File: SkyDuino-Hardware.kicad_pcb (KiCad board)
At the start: 4 copper layers, 123 x 56 mm, 75 parts, among them J1 24V, J11 DBG, J12 USB-A RMT, J13 DISP, J14 USB_C Artisan, J2 BT, J4 Drum, J5 Exhaust, J6 Cooling, J7 Cooling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

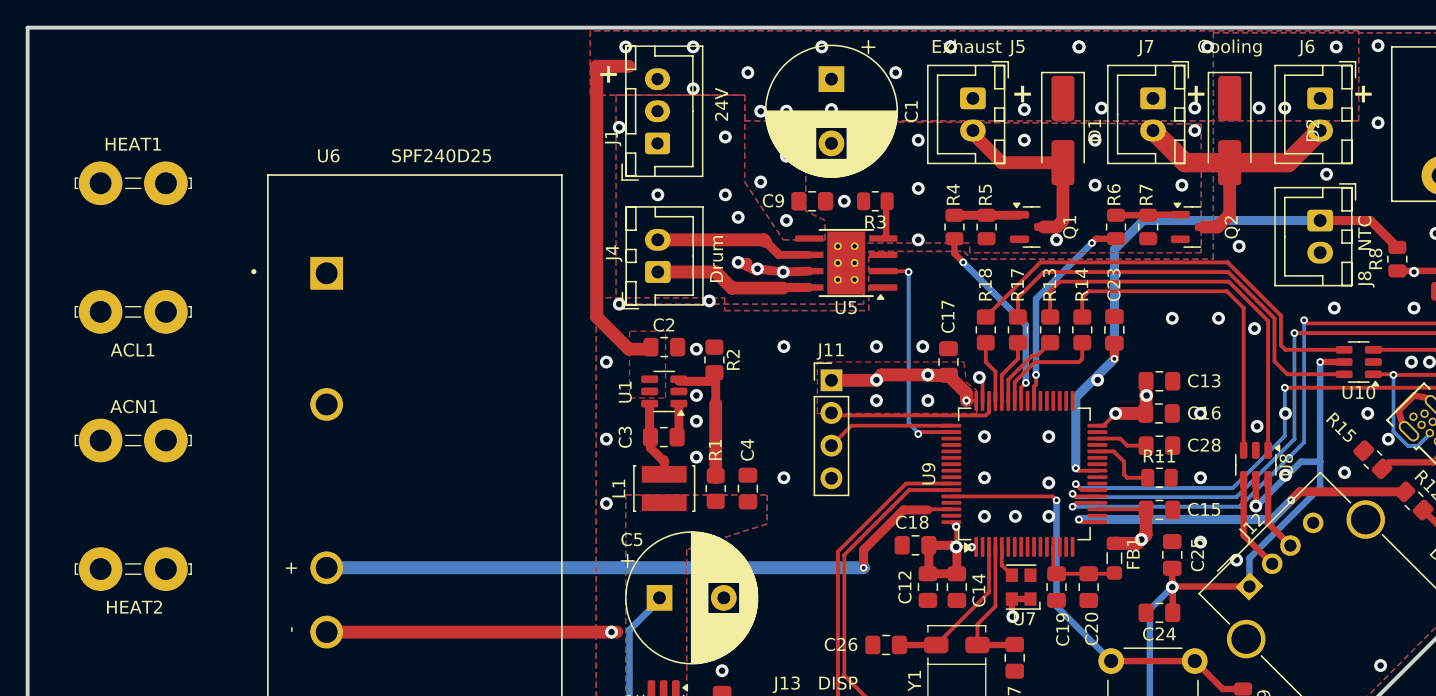
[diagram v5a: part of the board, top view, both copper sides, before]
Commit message: Label AC lines
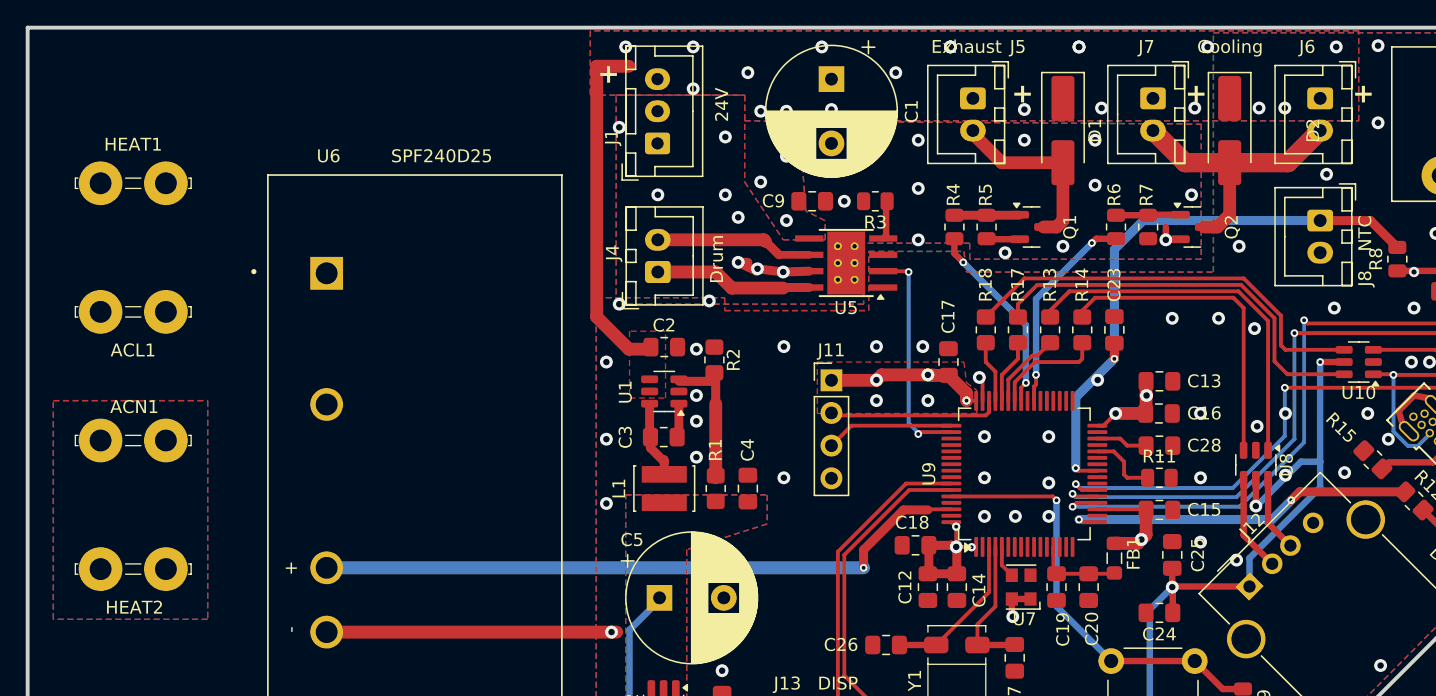
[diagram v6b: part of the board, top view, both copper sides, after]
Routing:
- net GND: track 32.5 -> 36.1 mm, vias 78 -> 79
- net Net-(R13-Pad1): track 30.6 -> 29.1 mm
- net Net-(R17-Pad1): track 32.9 -> 31.8 mm
- net Net-(R18-Pad1): track 33.8 -> 32.8 mm
- net Net-(R14-Pad1): track 25.9 -> 24.9 mm
- added copper zone on B.Cu, net Net-(ACN1-Pin_1)
- added copper zone on F.Cu, net Net-(ACN1-Pin_1)
- added copper zone on In1.Cu, net Net-(ACN1-Pin_1)
- added copper zone on In2.Cu, net Net-(ACN1-Pin_1)

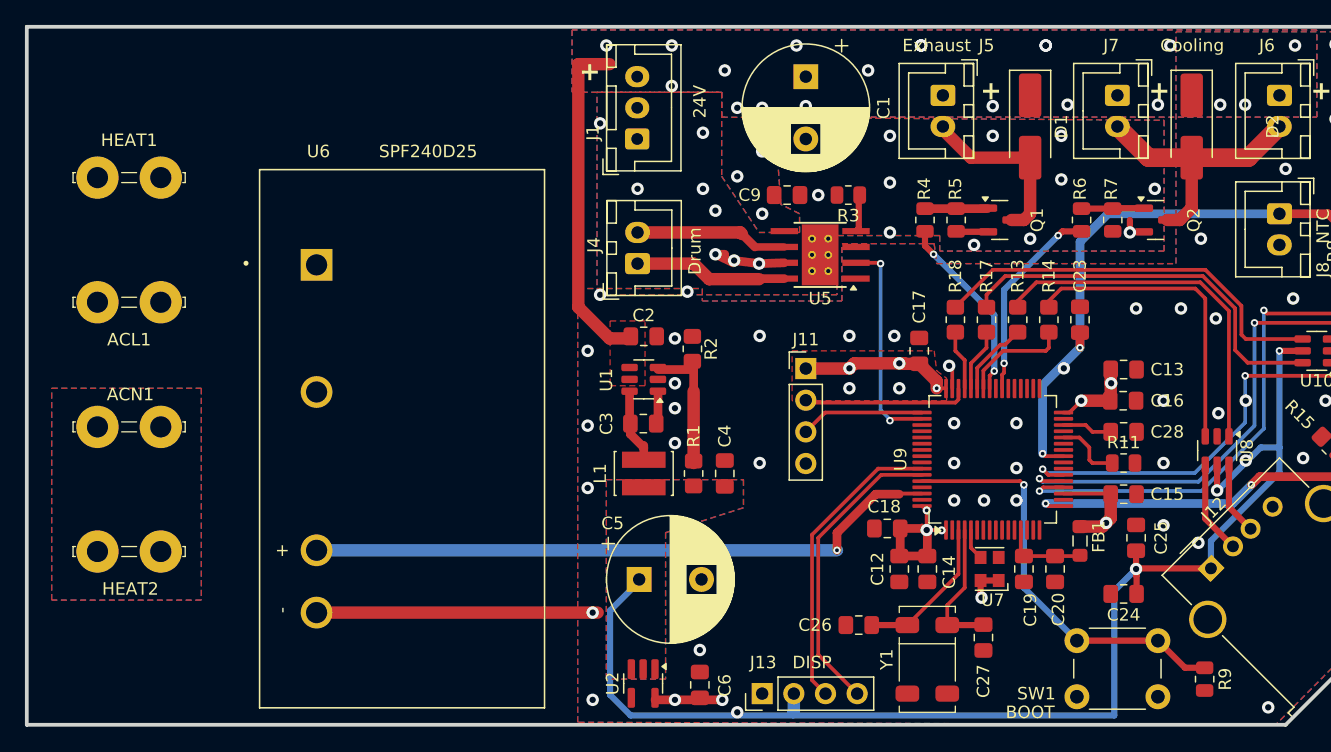
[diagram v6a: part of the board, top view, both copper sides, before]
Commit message: Pour AC lines
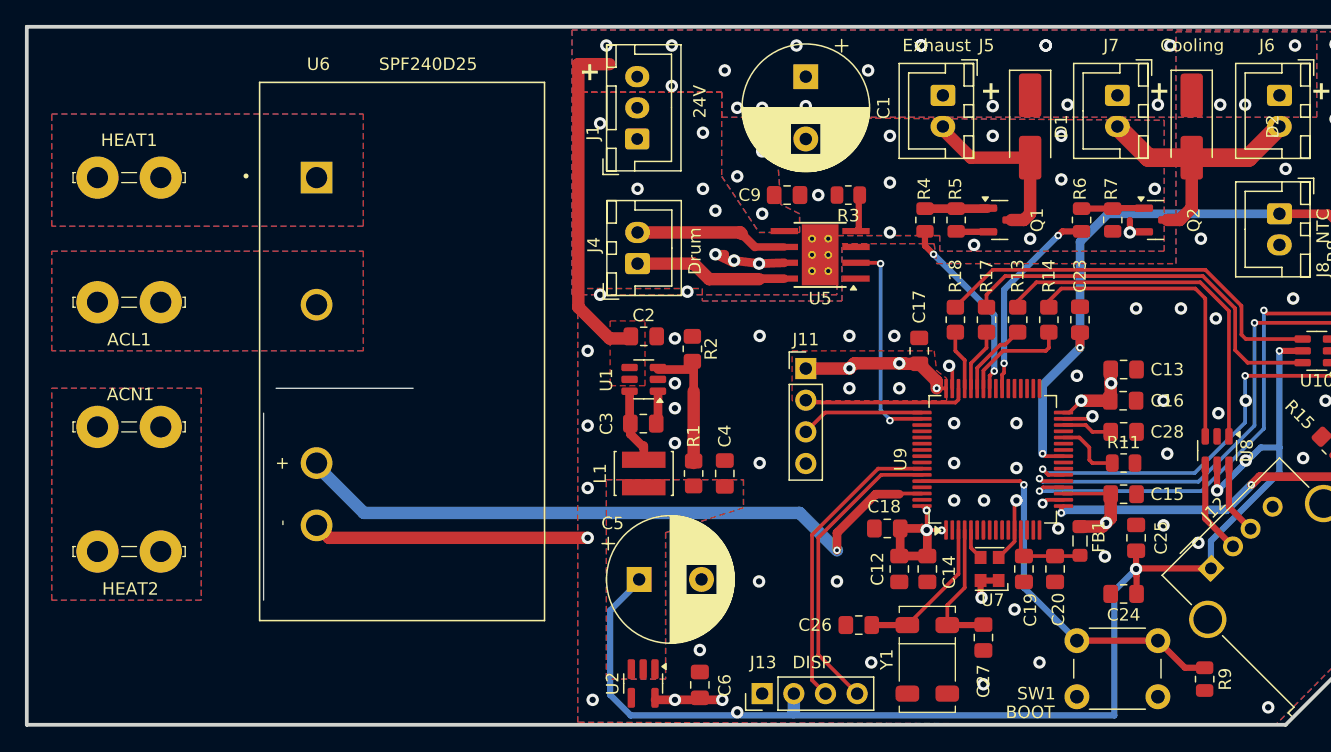
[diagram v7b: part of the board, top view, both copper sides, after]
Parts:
- moved U6 7.00 mm to (129.2, 106.0)
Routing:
- net GND: track 36.1 -> 45.4 mm, vias 79 -> 89
- net SSR: track 51.3 -> 54.3 mm
- net LED0: track 27.7 -> 25.9 mm
- added copper zone on B.Cu, net Net-(ACL1-Pin_1)
- added copper zone on F.Cu, net Net-(ACL1-Pin_1)
- added copper zone on In1.Cu, net Net-(ACL1-Pin_1)
- added copper zone on In2.Cu, net Net-(ACL1-Pin_1)
- added copper zone on B.Cu, net Net-(HEAT1-Pin_1)
- added copper zone on F.Cu, net Net-(HEAT1-Pin_1)
- added copper zone on In1.Cu, net Net-(HEAT1-Pin_1)
- added copper zone on In2.Cu, net Net-(HEAT1-Pin_1)
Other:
- outline, holes or cut-outs redrawn

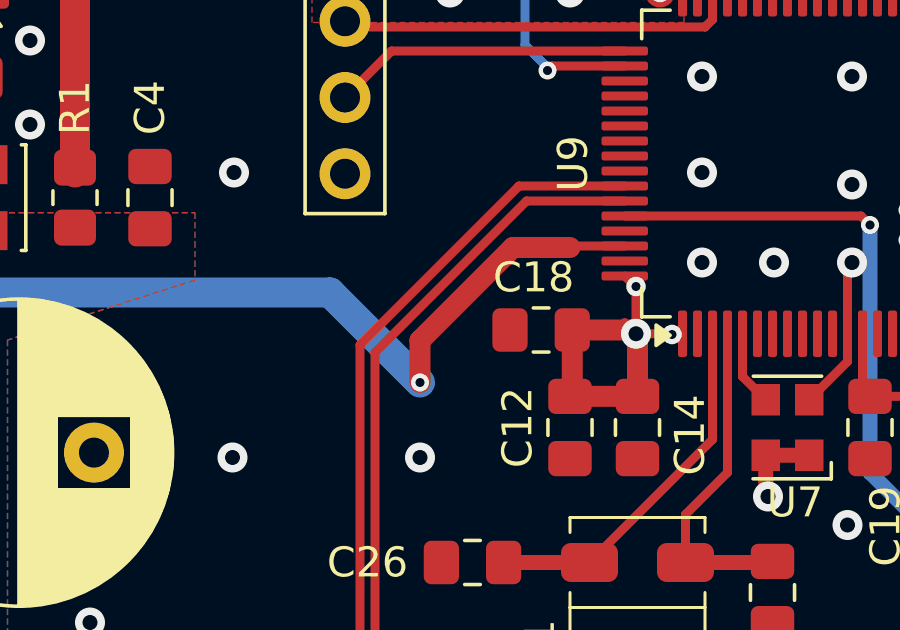
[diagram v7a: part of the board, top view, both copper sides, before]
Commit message: Fix DRC vialations
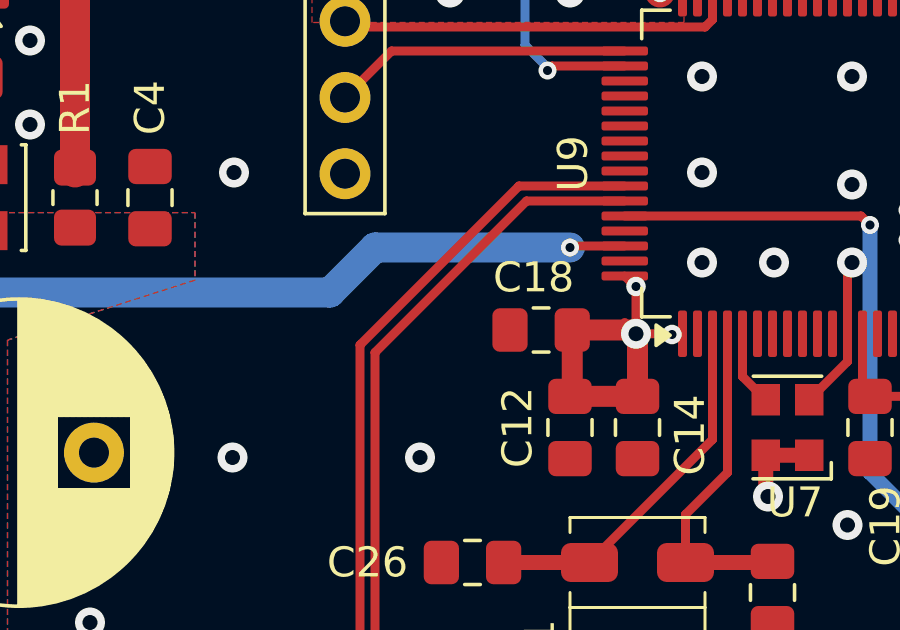
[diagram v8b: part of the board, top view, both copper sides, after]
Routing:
- net SSR: track 54.3 -> 51.0 mm
